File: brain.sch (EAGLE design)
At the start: 9 parts

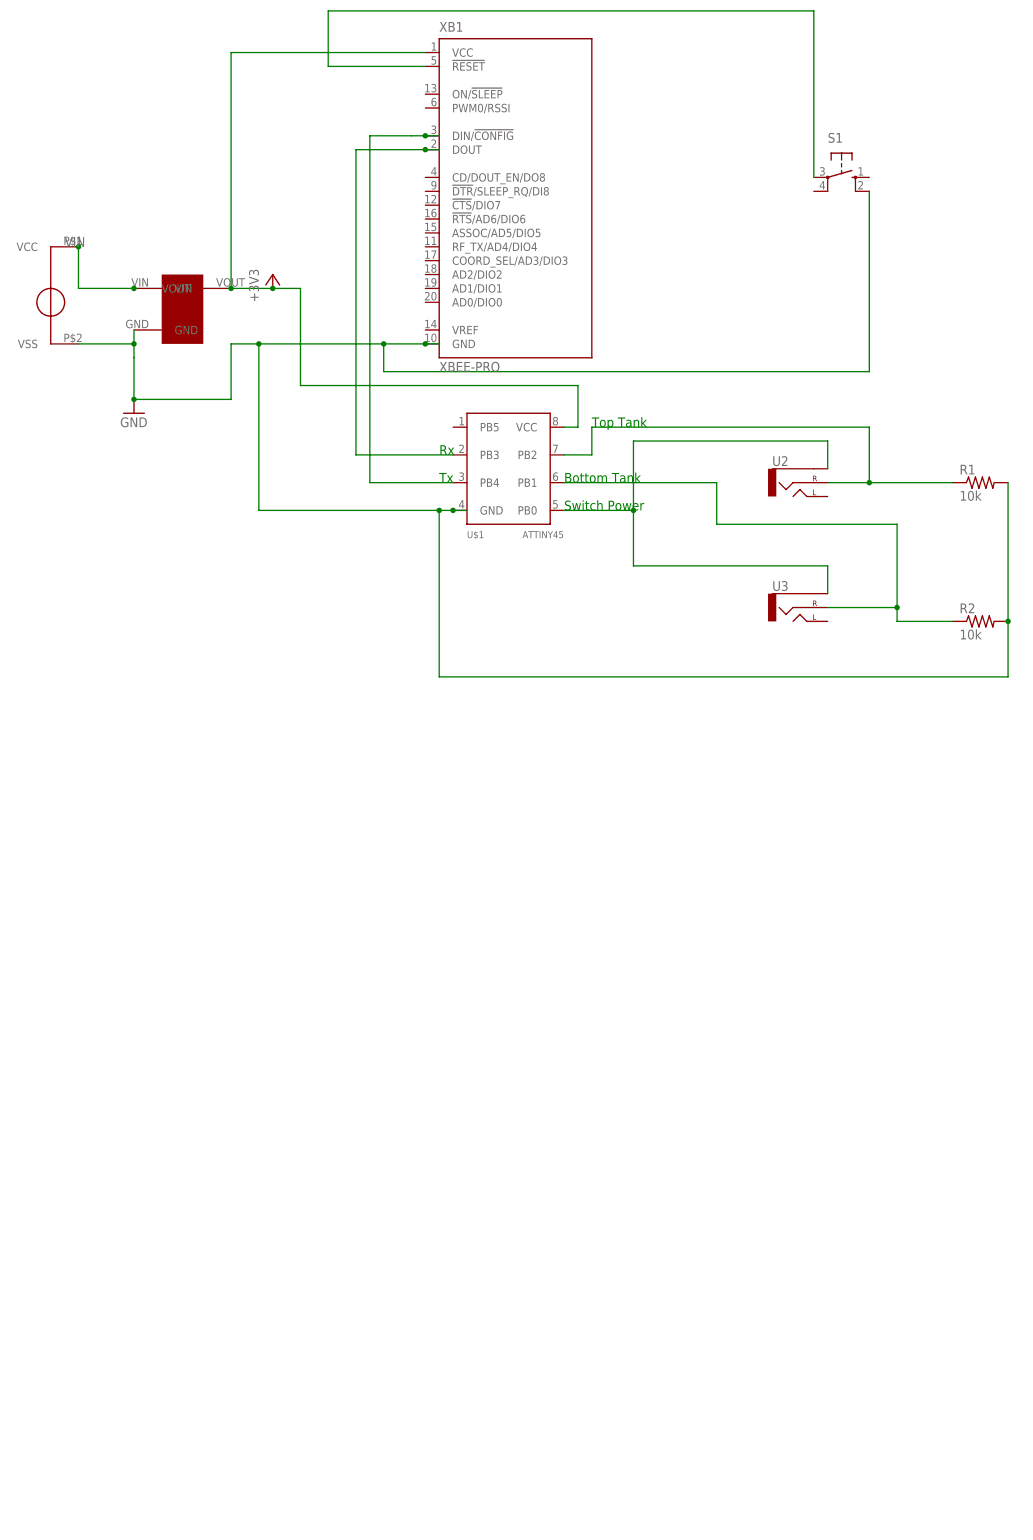
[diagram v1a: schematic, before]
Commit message: Added the receiver to schematic and board. Quick layout of the board.
TODO: Add bypass caps, figure out what the output of the receiver will
be (LED? something else? should we just make like through holes
for the ouput of the tiny and the supply and gnd so we can change it
on the fly?)
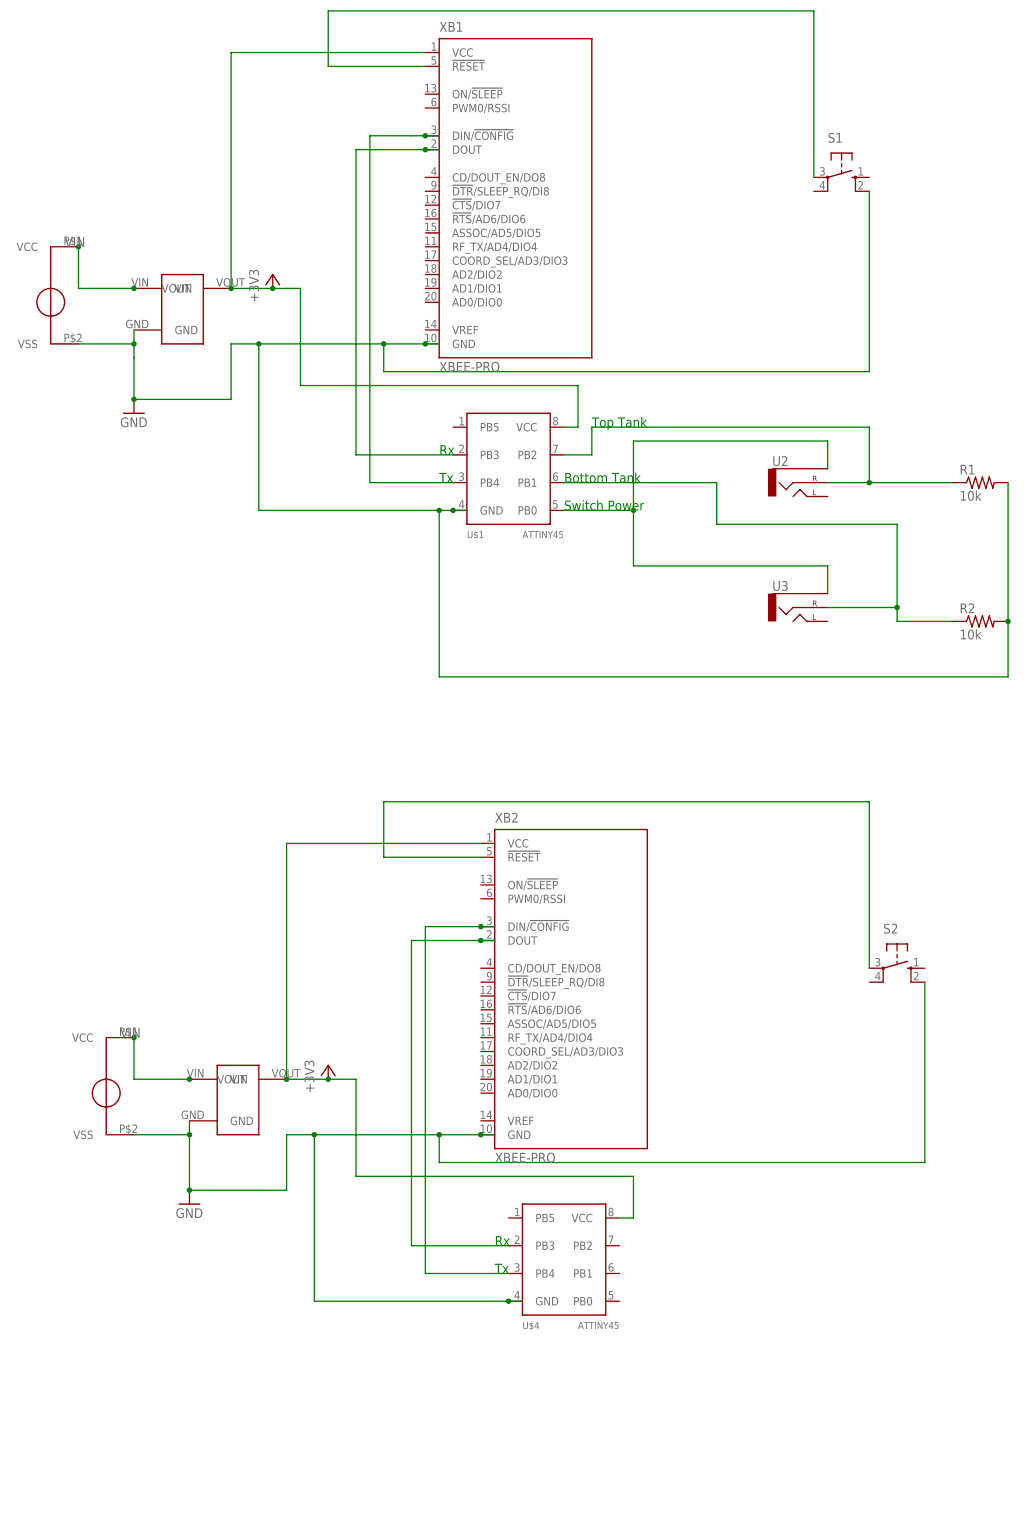
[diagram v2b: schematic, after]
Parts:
- added S2: (no value), switch-omron:10-XX
- added U$4: ATTINY45, attiny45:ATTINY45
- added U$5: LP2950, seniordesign:LP2950
- added U$6: SUNNYBUDDYMOUNT, seniordesign:SUNNYBUDDYMOUNT
- added XB2: XBEE-PRO, maxstream:XBEE-PRO
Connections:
- new net N$7: U$4.PB4, XB2.DIN/!CONFIG
- new net N$8: S2.P, XB2.!RESET
- new net N$9: U$4.PB3, XB2.DOUT
- net +3V3: now also U$4.VCC, U$5.VOUT, XB2.VCC
- net GND: now also S2.S1, U$4.GND, U$5.GND, U$6.VSS, XB2.GND
- net VIN: now also U$5.VIN, U$6.VCC
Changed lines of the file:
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@@
 <part name="+3V1" library="supply1" deviceset="+3V3" device=""/>
 <part name="U$3" library="seniordesign" deviceset="SUNNYBUDDYMOUNT" device=""/>
+<part name="XB2" library="maxstream" deviceset="XBEE" device="-PRO">
+<attribute name="MPN" value=""/>
+<attribute name="OC_NEWARK" value="unknown"/>
+</part>
+<part name="U$4" library="attiny45" deviceset="ATTINY45" device="">
+<attribute name="MF" value=""/>
+<attribute name="MPN" value=""/>
+<attribute name="OC_NEWARK" value="unknown"/>
+</part>
+<part name="S2" library="switch-omron" deviceset="10-XX" device=""/>
+<part name="GND2" library="supply1" deviceset="GND" device=""/>
+<part name="U$5" library="seniordesign" deviceset="LP2950" device=""/>
+<part name="+3V2" library="supply1" deviceset="+3V3" device=""/>
+<part name="U$6" library="seniordesign" deviceset="SUNNYBUDDYMOUNT" device=""/>
 </parts>
 <sheets>
@@
 <text x="86.36" y="-10.16" size="1.778" layer="91">Bottom Tank</text>
 <text x="91.44" y="0" size="1.778" layer="91">Top Tank</text>
+<text x="73.66" y="-154.94" size="1.778" layer="91">Tx</text>
+<text x="73.66" y="-149.86" size="1.778" layer="91">Rx</text>
 </plain>
 <instances>
@@
 <instance part="+3V1" gate="G$1" x="33.02" y="27.94"/>
 <instance part="U$3" gate="G$1" x="-7.62" y="25.4"/>
+<instance part="XB2" gate="G$1" x="86.36" y="-101.6"/>
+<instance part="U$4" gate="G$1" x="86.36" y="-152.4">
+<attribute name="OC_NEWARK" x="86.36" y="-152.4" size="1.778" layer="96" display="off"/>
+<attribute name="MF" x="86.36" y="-152.4" size="1.778" layer="96" display="off"/>
+<attribute name="MPN" x="86.36" y="-152.4" size="1.778" layer="96" display="off"/>
+</instance>
+<instance part="S2" gate="1" x="147.32" y="-99.06" rot="R270"/>
+<instance part="GND2" gate="1" x="17.78" y="-142.24"/>
+<instance part="U$5" gate="G$1" x="27.94" y="-124.46"/>
+<instance part="+3V2" gate="G$1" x="43.18" y="-116.84"/>
+<instance part="U$6" gate="G$1" x="2.54" y="-119.38"/>
 </instances>
 <busses>
@@
 <junction x="7.62" y="15.24"/>
 </segment>
+<segment>
+<wire x1="35.56" y1="-129.54" x2="40.64" y2="-129.54" width="0.1524" layer="91"/>
+<wire x1="73.66" y1="-129.54" x2="71.12" y2="-129.54" width="0.1524" layer="91"/>
+<wire x1="71.12" y1="-129.54" x2="63.5" y2="-129.54" width="0.1524" layer="91"/>
+<wire x1="63.5" y1="-129.54" x2="40.64" y2="-129.54" width="0.1524" layer="91"/>
+<wire x1="40.64" y1="-129.54" x2="40.64" y2="-160.02" width="0.1524" layer="91"/>
+<wire x1="40.64" y1="-160.02" x2="76.2" y2="-160.02" width="0.1524" layer="91"/>
+<wire x1="76.2" y1="-160.02" x2="78.74" y2="-160.02" width="0.1524" layer="91"/>
+<pinref part="S2" gate="1" pin="S1"/>
+<wire x1="152.4" y1="-101.6" x2="152.4" y2="-134.62" width="0.1524" layer="91"/>
+<wire x1="152.4" y1="-134.62" x2="63.5" y2="-134.62" width="0.1524" layer="91"/>
+<wire x1="63.5" y1="-134.62" x2="63.5" y2="-129.54" width="0.1524" layer="91"/>
+<junction x="40.64" y="-129.54"/>
+<junction x="63.5" y="-129.54"/>
+<wire x1="17.78" y1="-127" x2="17.78" y2="-129.54" width="0.1524" layer="91"/>
+<wire x1="17.78" y1="-129.54" x2="17.78" y2="-139.7" width="0.1524" layer="91"/>
+<wire x1="17.78" y1="-139.7" x2="35.56" y2="-139.7" width="0.1524" layer="91"/>
+<wire x1="35.56" y1="-139.7" x2="35.56" y2="-129.54" width="0.1524" layer="91"/>
+<pinref part="GND2" gate="1" pin="GND"/>
+<junction x="17.78" y="-139.7"/>
+<pinref part="U$5" gate="G$1" pin="GND"/>
+<pinref part="XB2" gate="G$1" pin="GND"/>
+<junction x="71.12" y="-129.54"/>
+<pinref part="U$4" gate="G$1" pin="GND"/>
+<junction x="76.2" y="-160.02"/>
+<pinref part="U$6" gate="G$1" pin="VSS"/>
+<wire x1="7.62" y1="-129.54" x2="17.78" y2="-129.54" width="0.1524" layer="91"/>
+<junction x="17.78" y="-129.54"/>
+</segment>
 </net>
 <net name="N$2" class="0">
@@
 <junction x="-2.54" y="33.02"/>
 <junction x="7.62" y="25.4"/>
+</segment>
+<segment>
+<wire x1="17.78" y1="-119.38" x2="7.62" y2="-119.38" width="0.1524" layer="91"/>
+<wire x1="7.62" y1="-119.38" x2="7.62" y2="-111.76" width="0.1524" layer="91"/>
+<label x="5.08" y="-111.76" size="1.778" layer="95"/>
+<pinref part="U$5" gate="G$1" pin="VIN"/>
+<pinref part="U$6" gate="G$1" pin="VCC"/>
+<junction x="7.62" y="-111.76"/>
+<junction x="17.78" y="-119.38"/>
 </segment>
 </net>
@@
 <junction x="33.02" y="25.4"/>
 </segment>
-</net>
+<segment>
+<pinref part="XB2" gate="G$1" pin="VCC"/>
+<wire x1="35.56" y1="-119.38" x2="35.56" y2="-76.2" width="0.1524" layer="91"/>
+<wire x1="35.56" y1="-76.2" x2="71.12" y2="-76.2" width="0.1524" layer="91"/>
+<pinref part="U$4" gate="G$1" pin="VCC"/>
+<wire x1="96.52" y1="-144.78" x2="99.06" y2="-144.78" width="0.1524" layer="91"/>
+<wire x1="99.06" y1="-144.78" x2="99.06" y2="-137.16" width="0.1524" layer="91"/>
+<wire x1="99.06" y1="-137.16" x2="48.26" y2="-137.16" width="0.1524" layer="91"/>
+<wire x1="48.26" y1="-137.16" x2="48.26" y2="-119.38" width="0.1524" layer="91"/>
+<wire x1="48.26" y1="-119.38" x2="43.18" y2="-119.38" width="0.1524" layer="91"/>
+<pinref part="U$5" gate="G$1" pin="VOUT"/>
+<junction x="35.56" y="-119.38"/>
+<pinref part="+3V2" gate="G$1" pin="+3V3"/>
+<wire x1="43.18" y1="-119.38" x2="35.56" y2="-119.38" width="0.1524" layer="91"/>
+<junction x="43.18" y="-119.38"/>
+</segment>
+</net>
+<net name="N$7" class="0">
+<segment>
+<pinref part="XB2" gate="G$1" pin="DIN/!CONFIG"/>
+<wire x1="71.12" y1="-91.44" x2="68.58" y2="-91.44" width="0.1524" layer="91"/>
+<wire x1="68.58" y1="-91.44" x2="60.96" y2="-91.44" width="0.1524" layer="91"/>
+<wire x1="60.96" y1="-91.44" x2="60.96" y2="-154.94" width="0.1524" layer="91"/>
+<pinref part="U$4" gate="G$1" pin="PB4"/>
+<wire x1="60.96" y1="-154.94" x2="76.2" y2="-154.94" width="0.1524" layer="91"/>
+<wire x1="71.12" y1="-91.44" x2="73.66" y2="-91.44" width="0.1524" layer="91"/>
+<junction x="71.12" y="-91.44"/>
+</segment>
+</net>
+<net name="N$8" class="0">
+<segment>
+<pinref part="XB2" gate="G$1" pin="!RESET"/>
+<wire x1="71.12" y1="-78.74" x2="53.34" y2="-78.74" width="0.1524" layer="91"/>
+<wire x1="53.34" y1="-78.74" x2="53.34" y2="-68.58" width="0.1524" layer="91"/>
+<pinref part="S2" gate="1" pin="P"/>
+<wire x1="53.34" y1="-68.58" x2="142.24" y2="-68.58" width="0.1524" layer="91"/>
+<wire x1="142.24" y1="-68.58" x2="142.24" y2="-99.06" width="0.1524" layer="91"/>
+</segment>
+</net>
+<net name="N$9" class="0">
+<segment>
+<pinref part="XB2" gate="G$1" pin="DOUT"/>
+<wire x1="71.12" y1="-93.98" x2="58.42" y2="-93.98" width="0.1524" layer="91"/>
+<wire x1="58.42" y1="-93.98" x2="58.42" y2="-149.86" width="0.1524" layer="91"/>
+<wire x1="73.66" y1="-93.98" x2="71.12" y2="-93.98" width="0.1524" layer="91"/>
+<pinref part="U$4" gate="G$1" pin="PB3"/>
+<wire x1="76.2" y1="-149.86" x2="58.42" y2="-149.86" width="0.1524" layer="91"/>
+<junction x="71.12" y="-93.98"/>
+</segment>
+</net>

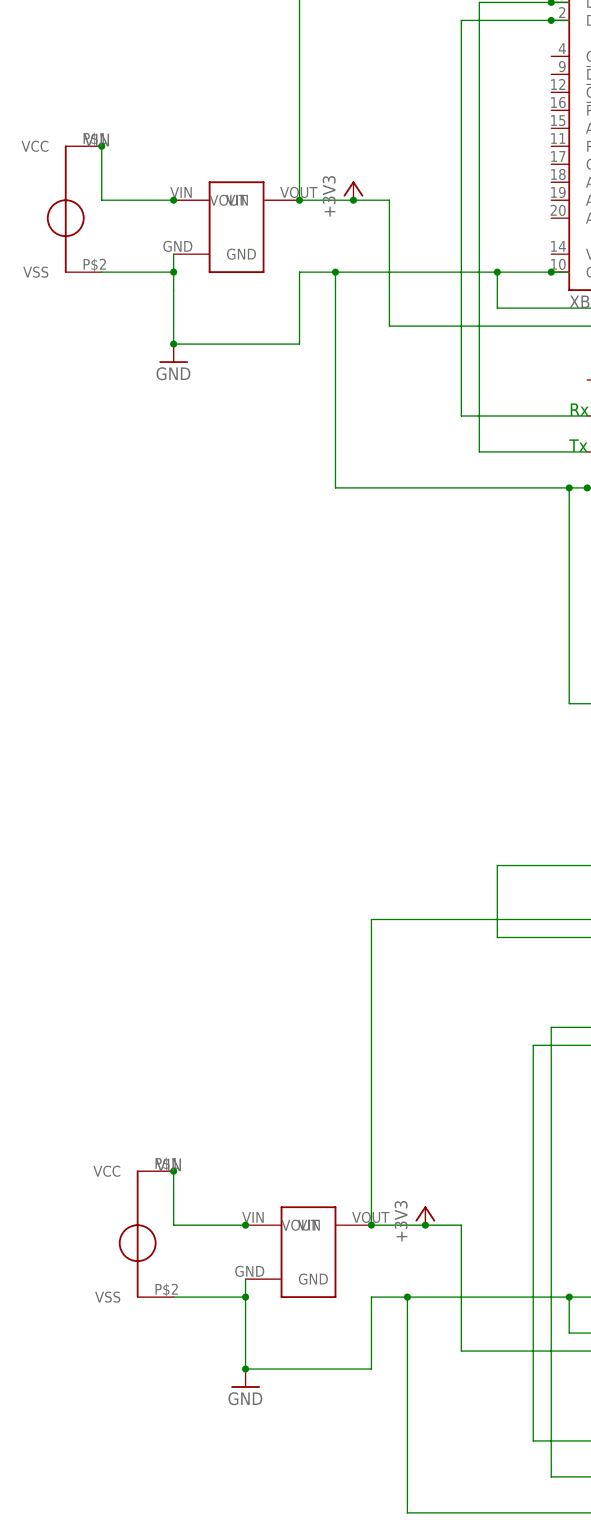
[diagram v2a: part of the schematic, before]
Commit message: Added some text to board, played a bit with layout/routing.
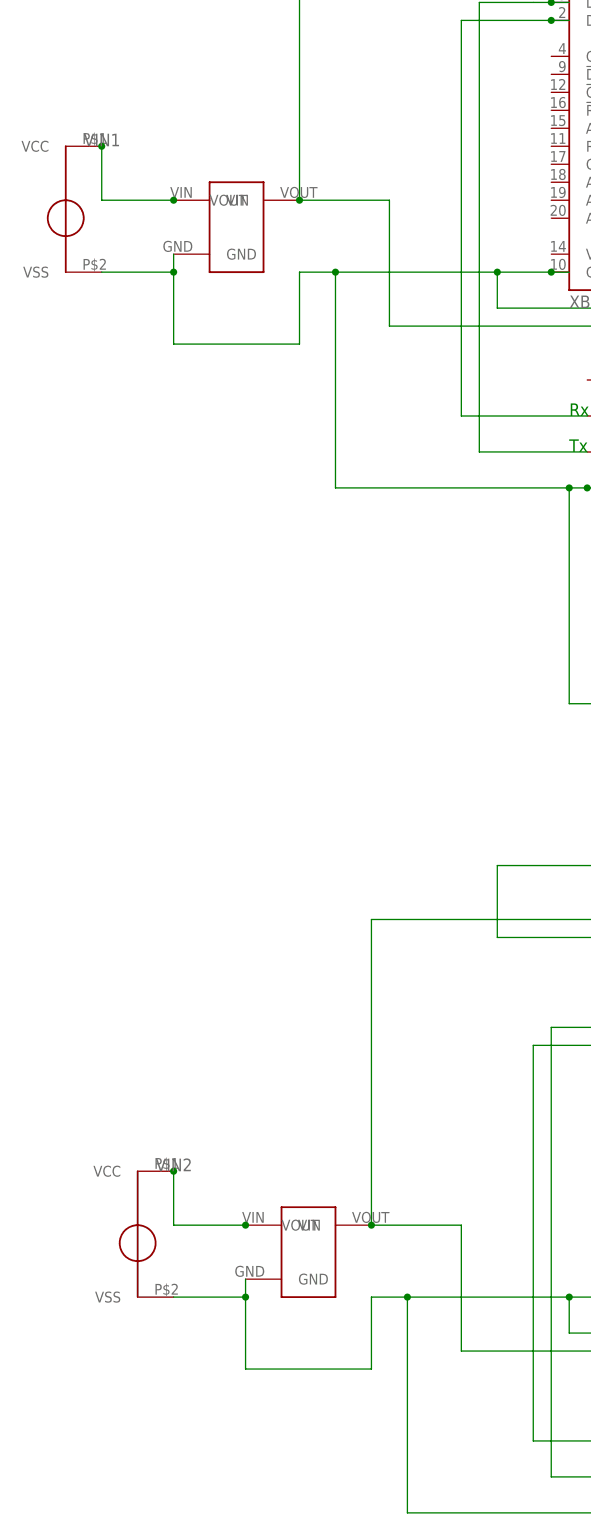
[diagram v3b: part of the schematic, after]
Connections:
- removed net +3V3: U$1.VCC, U$2.VOUT, U$4.VCC, U$5.VOUT, XB1.VCC, XB2.VCC
- removed net GND: R1.2, R2.2, S1.S1, S2.S1, U$1.GND, U$2.GND, U$3.VSS, U$4.GND, U$5.GND, U$6.VSS, XB1.GND, XB2.GND
- removed net VIN: U$2.VIN, U$3.VCC, U$5.VIN, U$6.VCC
- new net GND1: R1.2, R2.2, S1.S1, U$1.GND, U$2.GND, U$3.VSS, XB1.GND
- new net GND2: S2.S1, U$4.GND, U$5.GND, U$6.VSS, XB2.GND
- new net VCC1: U$1.VCC, U$2.VOUT, XB1.VCC
- new net VIN1: U$2.VIN, U$3.VCC
- new net VIN2: U$5.VIN, U$6.VCC
- new net VOUT2: U$4.VCC, U$5.VOUT, XB2.VCC
